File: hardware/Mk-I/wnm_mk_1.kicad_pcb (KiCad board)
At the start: 2 copper layers, 96.5 x 66 mm, 122 parts, among them CON1 USB-MICRO-B, SW1 SW_PUSH, SW10 SW_PUSH, SW11 SW_PUSH, SW12 SW_PUSH, SW13 SW_PUSH, SW14 SW_PUSH, SW15 SW_PUSH, SW16 SW_PUSH, SW18 SW_PUSH, SW19 SW_PUSH, SW2 SW_PUSH, SW20 SW_PUSH, SW21 SW_PUSH, SW22 SW_PUSH, SW3 SW_PUSH, SW4 SW_PUSH, SW5 SW_PUSH, SW6 SW_PUSH, SW7 SW_PUSH, SW8 SW_PUSH, SW9 SW_PUSH, U10 STM32_SWD_Connector, U2 MCP73831, U3 BD33IA5, U4 STM32F407VG, U5 SGTL5000, U6 encoder_and_switch, U7 encoder_and_switch, U8 MOLEX_microSD_47219-2001, U9 SSD1306, X1 CRYSTAL

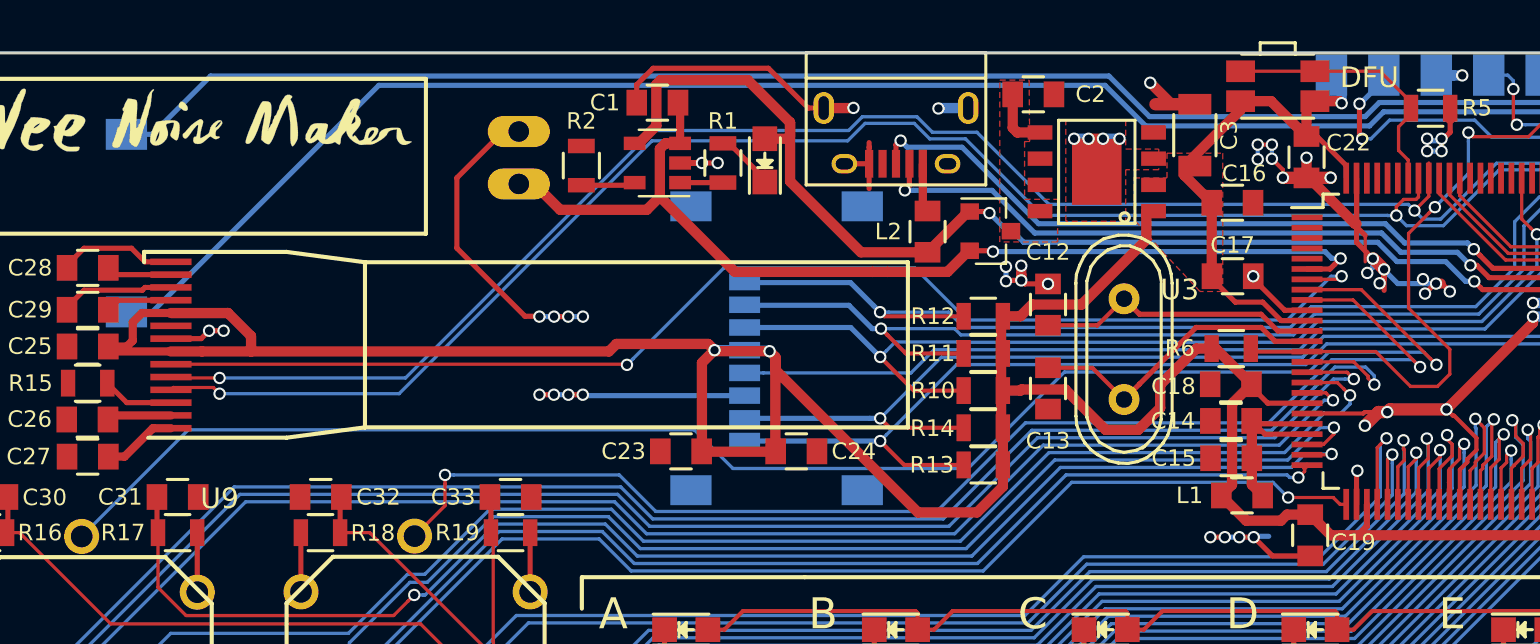
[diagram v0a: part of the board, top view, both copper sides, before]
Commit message: HW: Add I2C debug/extension connector
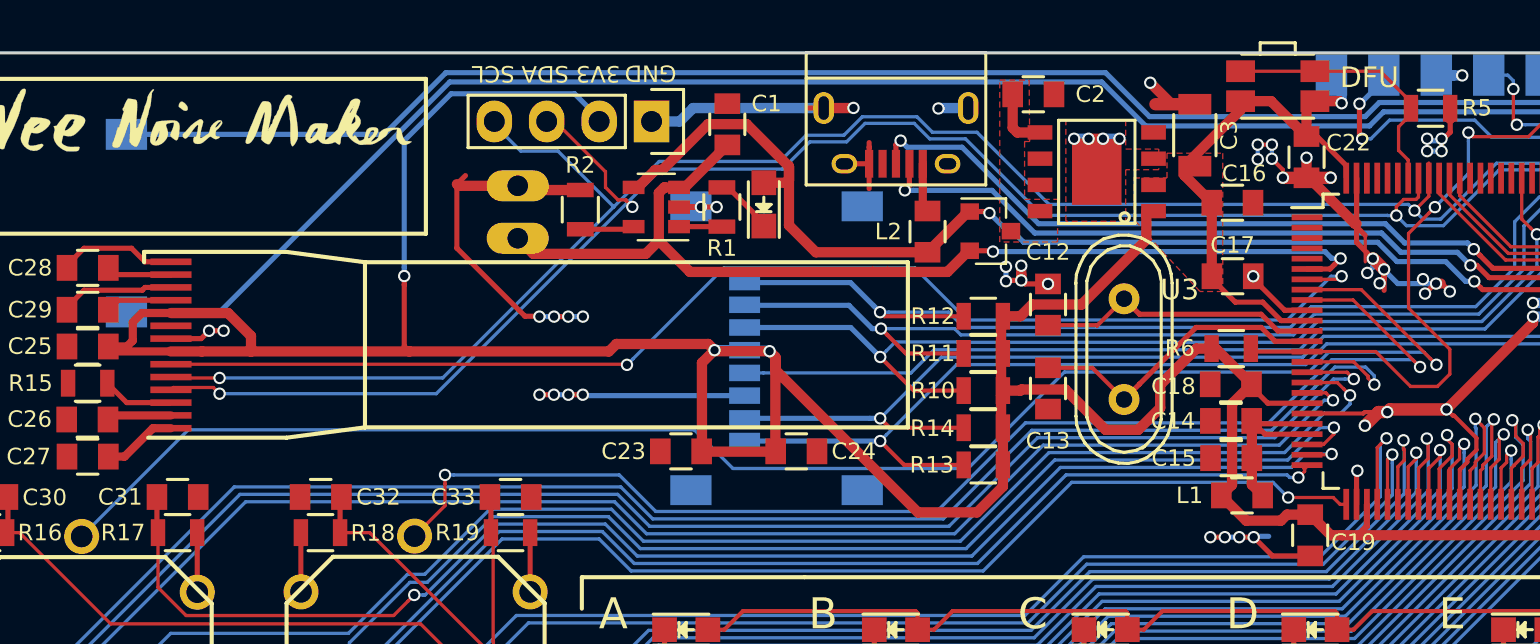
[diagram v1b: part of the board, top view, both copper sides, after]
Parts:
- added ext1: CONN_01X04, Socket_Strips:Socket_Strip_Straight_1x04, F.Cu at (116.4, 82.1)
- moved C1 3.55 mm to (120.1, 82.2), turned to 90 degrees
- moved BT1 2.63 mm to (109.9, 86.5)
- moved R1 2.13 mm to (119.8, 86.2)
- moved BAT1 2.13 mm to (121.9, 86.1)
- moved R2 2.13 mm to (113.0, 86.3)
- moved U2 2.13 mm to (116.7, 86.2)
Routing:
- net 3V3: track 224.8 -> 246.2 mm, vias 5 -> 6
- net Audio_SCL: track 97.4 -> 105.0 mm
- net Audio_SDA: track 98.2 -> 104.8 mm, vias 3 -> 4
- net VBUS: track 60.6 -> 58.6 mm
- net GND: track 174.3 -> 175.8 mm
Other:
- board text added: "3V3"
- board text added: "SCL"
- board text added: "SDA"
- board text added: "VBAT"

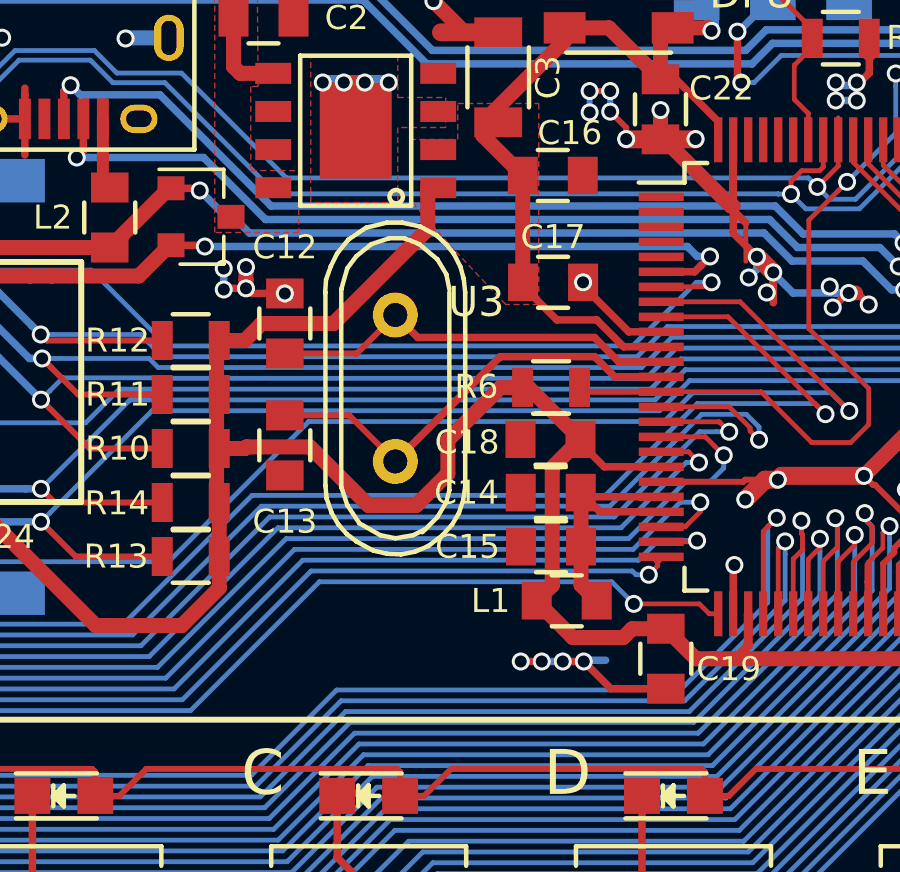
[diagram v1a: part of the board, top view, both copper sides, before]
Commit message: HW: Improve oscillator layout
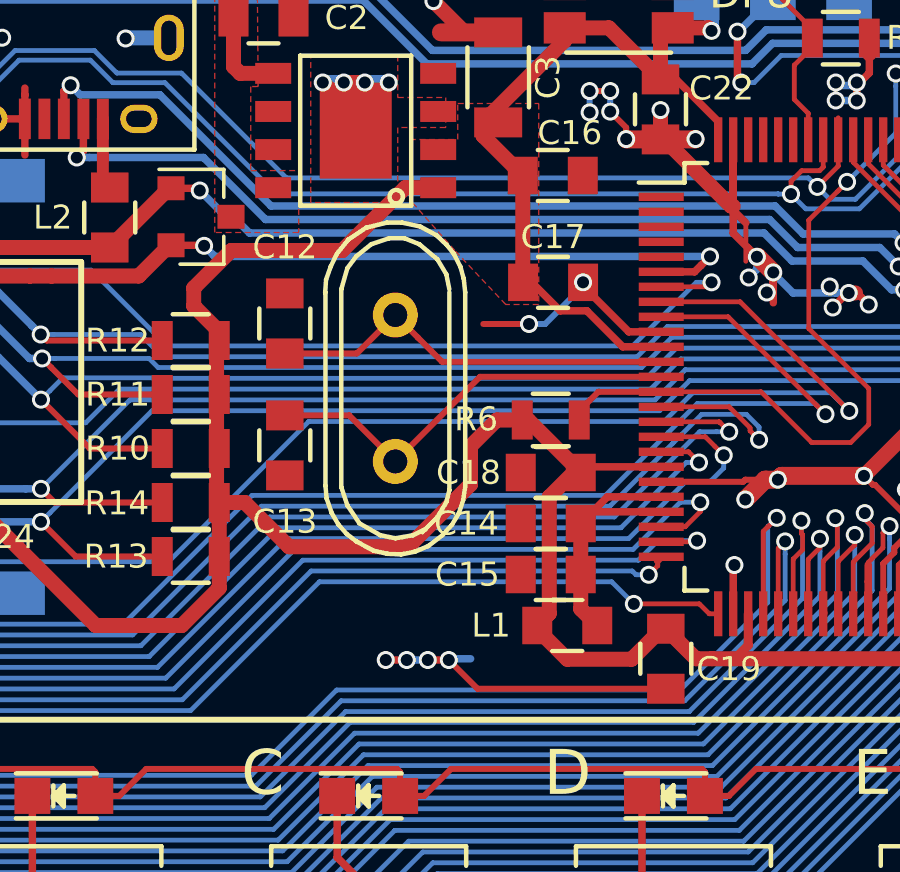
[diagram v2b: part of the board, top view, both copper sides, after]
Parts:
- C12, C13: value 22pF -> 20pF
- moved C18 1.11 mm to (144.5, 95.9)
- moved R6 1.08 mm to (144.5, 94.2)
- moved C14 1.03 mm to (144.5, 97.6)
- moved C15 0.93 mm to (144.5, 99.3)
- moved L1 0.82 mm to (145.1, 101.0)
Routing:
- net GND: track 175.8 -> 180.9 mm, vias 84 -> 80
- net 3V3: track 246.2 -> 247.4 mm
- net Net-(C13-Pad2): track 15.0 -> 14.4 mm
- net Net-(C12-Pad2): track 14.3 -> 13.7 mm
- net NRST: track 32.5 -> 33.0 mm

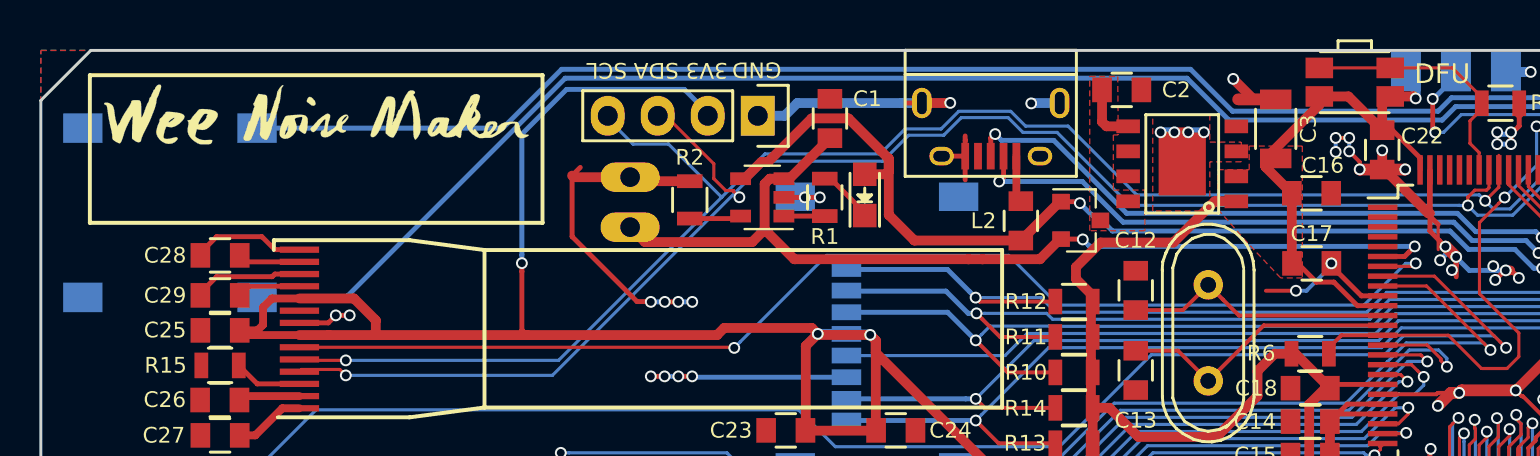
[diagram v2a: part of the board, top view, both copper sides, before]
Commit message: HW: Divide VBAT before connecting to the MCU
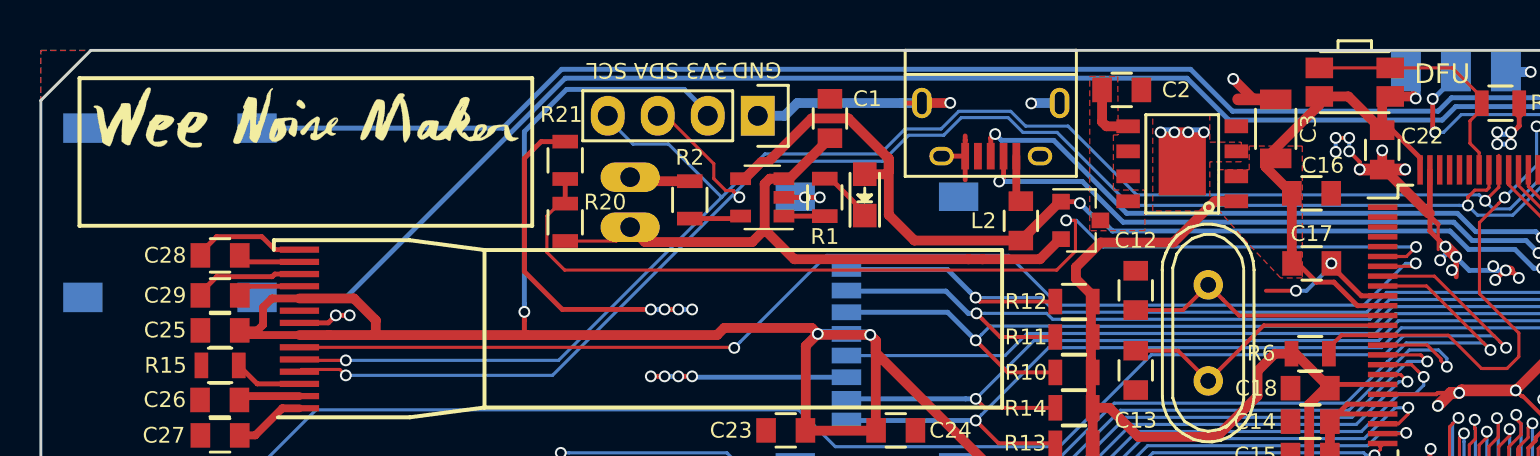
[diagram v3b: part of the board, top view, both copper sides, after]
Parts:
- added R20: 10K, Resistors_SMD:R_0805, F.Cu at (106.7, 87.5)
- added R21: 10K, Resistors_SMD:R_0805, F.Cu at (106.7, 84.3)
- moved G*** 0.55 mm to (93.5, 85.7)
- moved G*** 0.55 mm to (93.5, 82.2)
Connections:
- U4 pad 6: VBAT -> VBAT_SENSE
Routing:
- net VBAT_SENSE: track 0.00 -> 54.6 mm, vias 0 -> 2
- net VBAT: track 50.3 -> 33.9 mm, vias 2 -> 0
- net GND: track 180.9 -> 184.3 mm

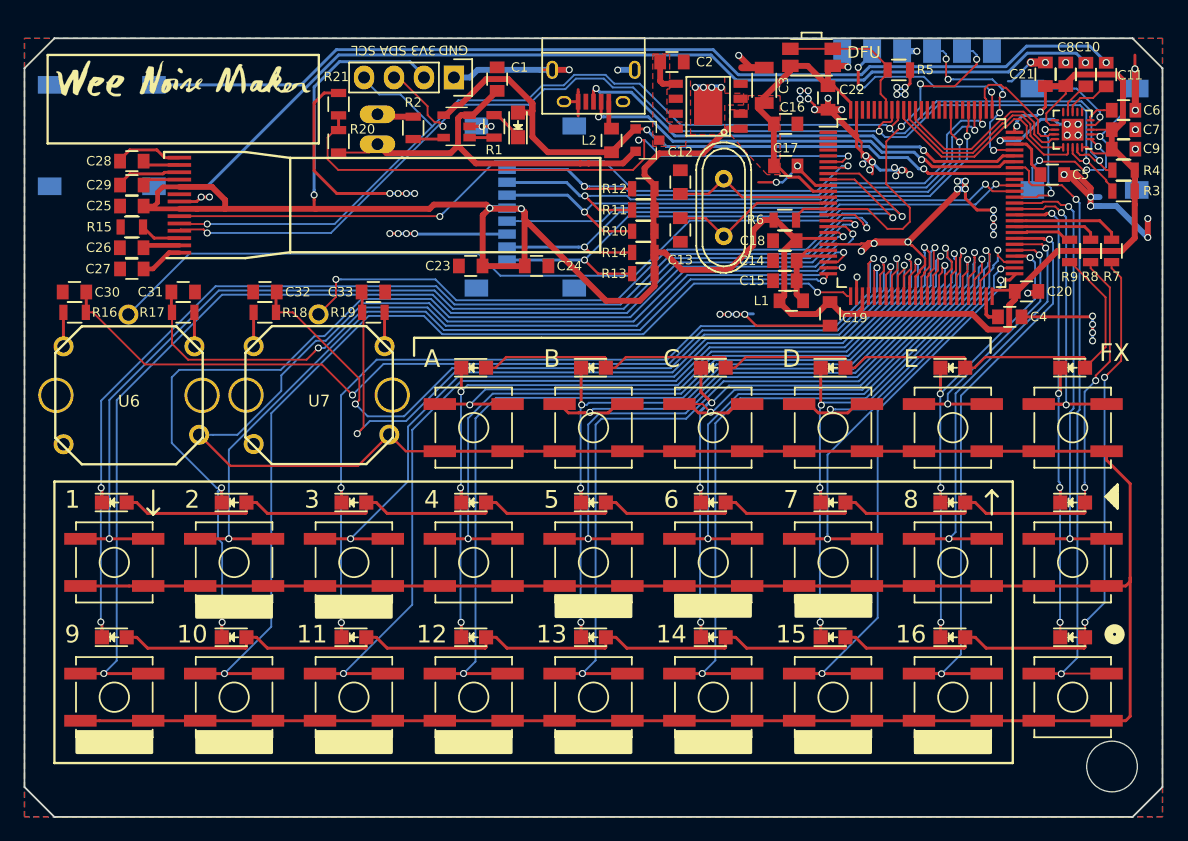
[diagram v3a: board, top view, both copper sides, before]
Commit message: HW: Increase board size
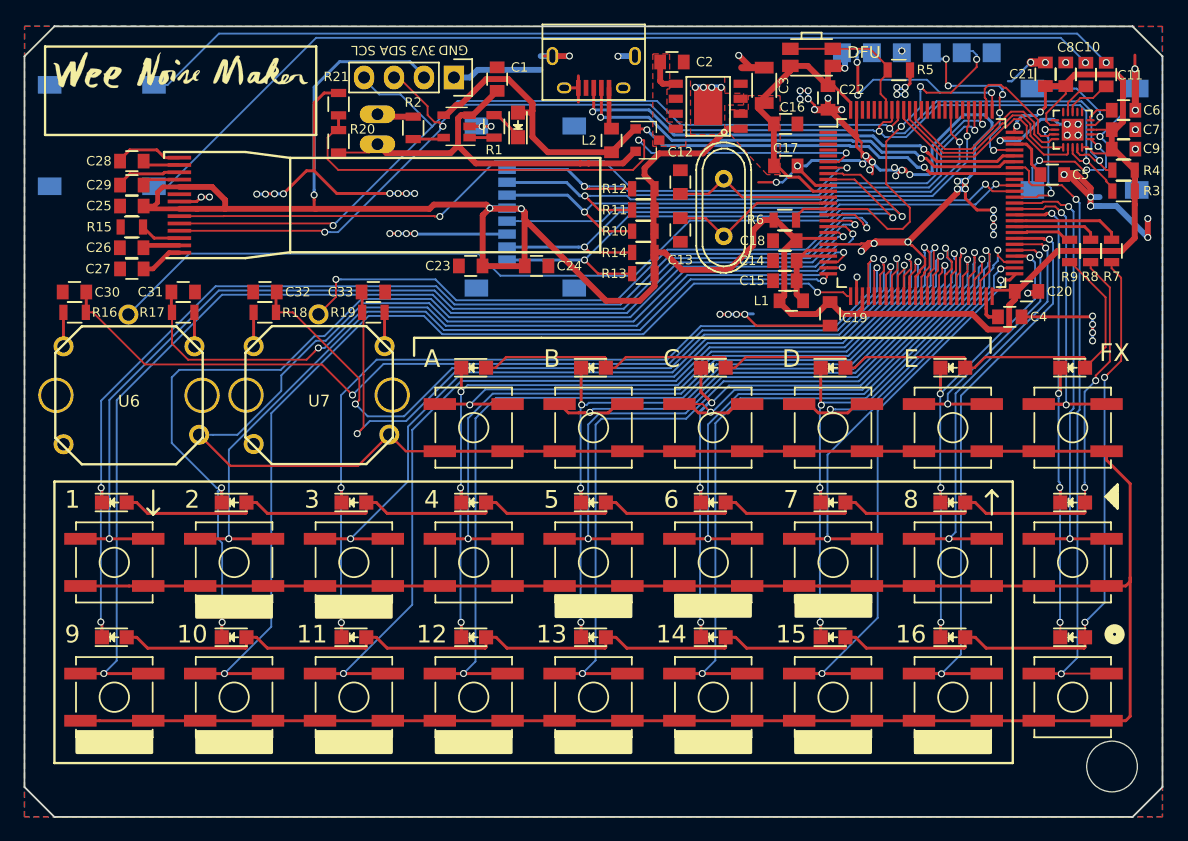
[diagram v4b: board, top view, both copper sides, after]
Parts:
- U10: footprint stm32f4-disco:STM32_SWD_Connector_SMD -> POSS:STM32_SWD_Connector_SMD
- moved CON1 1.17 mm to (128.3, 81.4)
- moved G*** 0.75 mm to (93.3, 84.9)
- moved G*** 0.75 mm to (93.3, 81.4)
- moved U10 0.15 mm to (146.8, 81.5)
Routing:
- net GND: track 184.3 -> 211.1 mm, vias 80 -> 84
- net Audio_SCL: track 105.0 -> 103.2 mm
- net Audio_SDA: track 104.8 -> 103.2 mm
- net SWCLK: track 17.3 -> 18.7 mm
- net Net-(CON1-Pad1): track 2.38 -> 3.54 mm
- net FS_DM: track 38.6 -> 39.5 mm
- net Net-(C11-Pad1): track 84.5 -> 83.6 mm
- net Net-(C10-Pad1): track 85.8 -> 85.1 mm
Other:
- board size 96.5 x 66 mm -> 96.5 x 67.1 mm

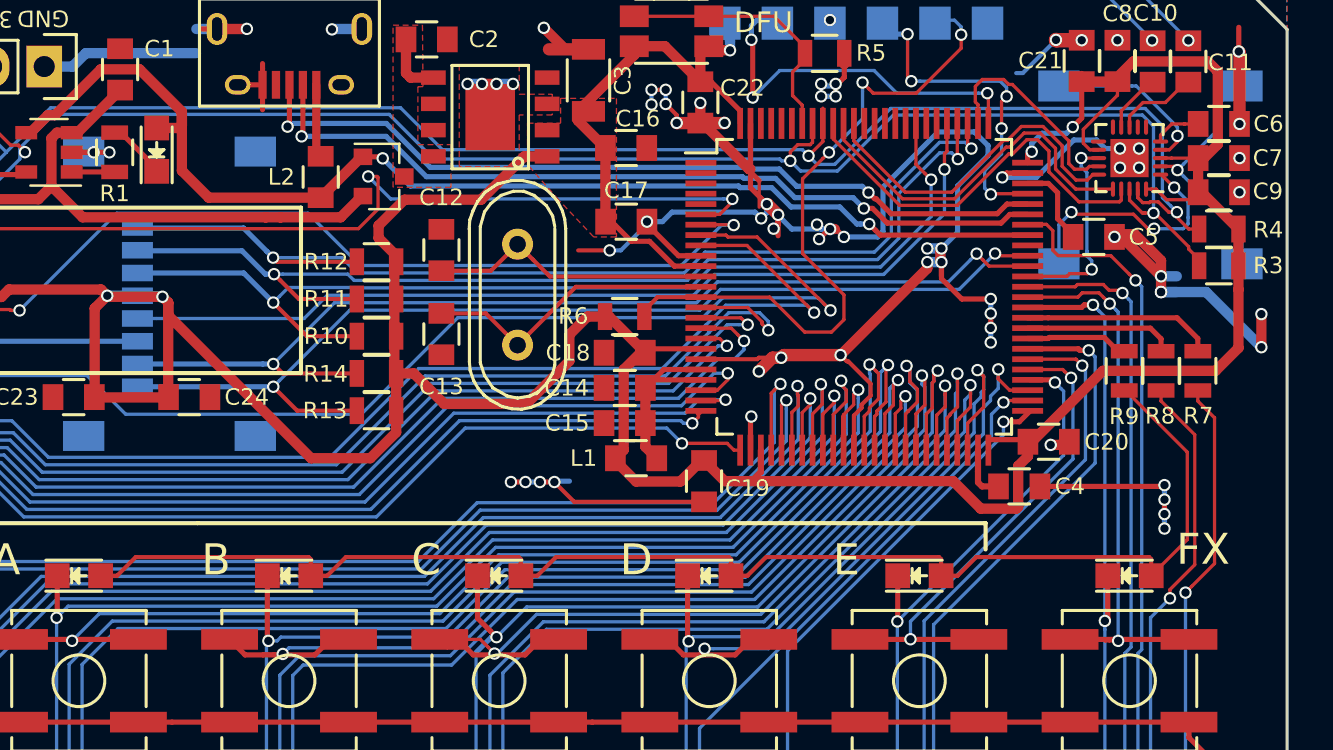
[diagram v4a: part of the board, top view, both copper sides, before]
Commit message: HW: Start rev-C with DAC VDDD fix
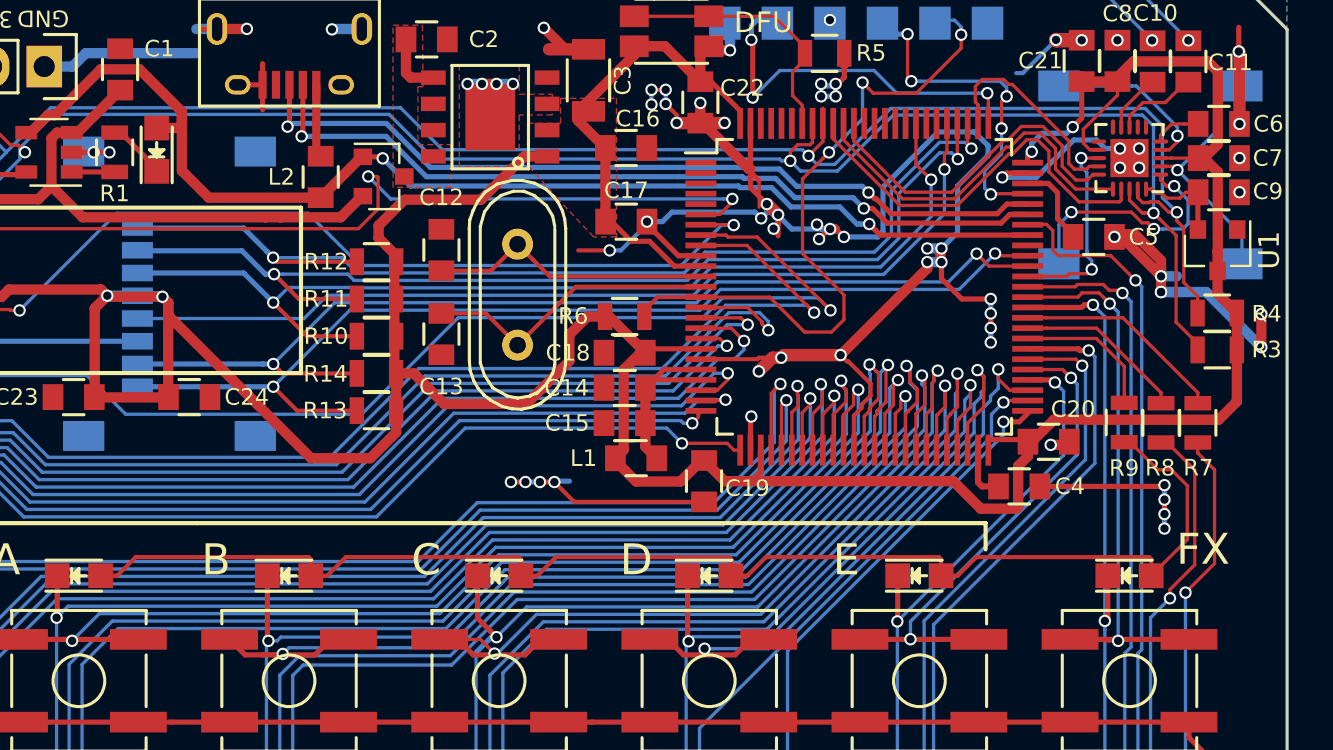
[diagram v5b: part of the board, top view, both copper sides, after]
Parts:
- added U1: AP7313-18-SR-G-7, TO_SOT_Packages_SMD:SOT-23, F.Cu at (173.2, 90.9)
- moved R4 4.06 mm to (173.2, 94.0)
- moved R3 4.06 mm to (173.2, 95.8)
- moved R7 2.51 mm to (172.2, 99.3)
- moved R8 2.51 mm to (170.4, 99.3)
- moved R9 2.50 mm to (168.7, 99.3)
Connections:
- C9 pad 1: 3V3 -> Net-(C9-Pad1)
- U5 pad 20: 3V3 -> Net-(C9-Pad1)
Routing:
- net Net-(C9-Pad1): track 0.00 -> 4.62 mm
- net Audio_SDA: track 103.2 -> 107.2 mm
- net Audio_SCL: track 103.2 -> 107.2 mm
- net Net-(D1-Pad2): track 124.8 -> 122.3 mm
- net Net-(D10-Pad2): track 113.3 -> 111.0 mm
- net ROW3: track 4.97 -> 7.00 mm
- net Net-(D20-Pad2): track 67.8 -> 65.9 mm
- net 3V3: track 247.0 -> 245.3 mm
- net ROW2: track 7.26 -> 8.25 mm
- net ROW1: track 9.26 -> 10.2 mm
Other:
- board text added: "Rev-C"
- board text removed: "Rev-B"
